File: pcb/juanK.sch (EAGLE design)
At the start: 56 parts, among them IC1 MEGA8-P, IC2 7805TV, T1 2N3904, T2 MCR106, T3 MCR106, T4 MCR106, T5 MCR106, T6 MCR106, T7 MCR106

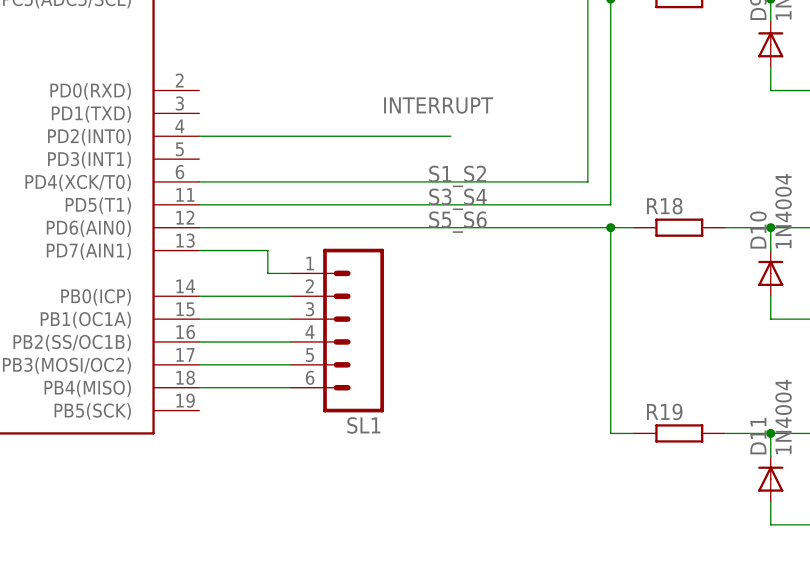
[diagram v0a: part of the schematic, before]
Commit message: Ordenar elementos y Optimizar caminos
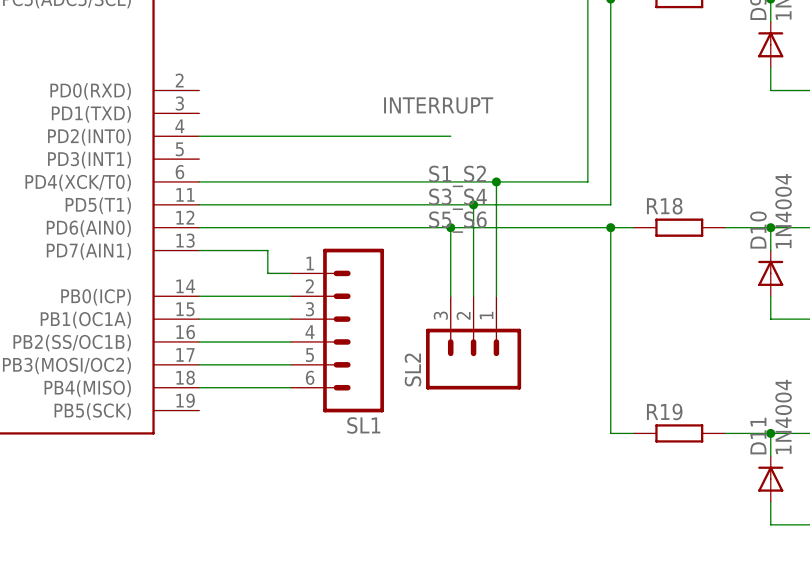
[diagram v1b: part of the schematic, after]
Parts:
- added SL2: (no value), con-amp-quick:M03
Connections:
- net S1_S2: now also SL2.1
- net S3_S4: now also SL2.2
- net S5_S6: now also SL2.3
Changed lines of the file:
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@@
 <?xml version="1.0" encoding="utf-8"?>
 <!DOCTYPE eagle SYSTEM "eagle.dtd">
-<eagle version="6.5.0">
+<eagle version="8.2.2">
 <drawing>
 <settings>
@@
 <grid distance="0.1" unitdist="inch" unit="inch" style="lines" multiple="1" display="no" altdistance="0.01" altunitdist="inch" altunit="inch"/>
 <layers>
-<layer number="1" name="Top" color="4" fill="1" visible="yes" active="no"/>
-<layer number="16" name="Bottom" color="1" fill="1" visible="yes" active="no"/>
-<layer number="17" name="Pads" color="2" fill="1" visible="yes" active="no"/>
-<layer number="18" name="Vias" color="2" fill="1" visible="yes" active="no"/>
-<layer number="19" name="Unrouted" color="6" fill="1" visible="yes" active="no"/>
-<layer number="20" name="Dimension" color="15" fill="1" visible="yes" active="no"/>
-<layer number="21" name="tPlace" color="7" fill="1" visible="yes" active="no"/>
-<layer number="22" name="bPlace" color="7" fill="1" visible="yes" active="no"/>
-<layer number="23" name="tOrigins" color="15" fill="1" visible="yes" active="no"/>
-<layer number="24" name="bOrigins" color="15" fill="1" visible="yes" active="no"/>
-<layer number="25" name="tNames" color="7" fill="1" visible="yes" active="no"/>
-<layer number="26" name="bNames" color="7" fill="1" visible="yes" active="no"/>
-<layer number="27" name="tValues" color="7" fill="1" visible="yes" active="no"/>
-<layer number="28" name="bValues" color="7" fill="1" visible="yes" active="no"/>
+<layer number="1" name="Top" color="4" fill="1" visible="no" active="no"/>
+<layer number="2" name="Route2" color="1" fill="3" visible="no" active="no"/>
+<layer number="3" name="Route3" color="4" fill="3" visible="no" active="no"/>
+<layer number="4" name="Route4" color="1" fill="4" visible="no" active="no"/>
+<layer number="5" name="Route5" color="4" fill="4" visible="no" active="no"/>
+<layer number="6" name="Route6" color="1" fill="8" visible="no" active="no"/>
+<layer number="7" name="Route7" color="4" fill="8" visible="no" active="no"/>
+<layer number="8" name="Route8" color="1" fill="2" visible="no" active="no"/>
+<layer number="9" name="Route9" color="4" fill="2" visible="no" active="no"/>
+<layer number="10" name="Route10" color="1" fill="7" visible="no" active="no"/>
+<layer number="11" name="Route11" color="4" fill="7" visible="no" active="no"/>
+<layer number="12" name="Route12" color="1" fill="5" visible="no" active="no"/>
+<layer number="13" name="Route13" color="4" fill="5" visible="no" active="no"/>
+<layer number="14" name="Route14" color="1" fill="6" visible="no" active="no"/>
+<layer number="15" name="Route15" color="4" fill="6" visible="no" active="no"/>
+<layer number="16" name="Bottom" color="1" fill="1" visible="no" active="no"/>
+<layer number="17" name="Pads" color="2" fill="1" visible="no" active="no"/>
+<layer number="18" name="Vias" color="2" fill="1" visible="no" active="no"/>
+<layer number="19" name="Unrouted" color="6" fill="1" visible="no" active="no"/>
+<layer number="20" name="Dimension" color="15" fill="1" visible="no" active="no"/>
+<layer number="21" name="tPlace" color="7" fill="1" visible="no" active="no"/>
+<layer number="22" name="bPlace" color="7" fill="1" visible="no" active="no"/>
+<layer number="23" name="tOrigins" color="15" fill="1" visible="no" active="no"/>
+<layer number="24" name="bOrigins" color="15" fill="1" visible="no" active="no"/>
+<layer number="25" name="tNames" color="7" fill="1" visible="no" active="no"/>
+<layer number="26" name="bNames" color="7" fill="1" visible="no" active="no"/>
+<layer number="27" name="tValues" color="7" fill="1" visible="no" active="no"/>
+<layer number="28" name="bValues" color="7" fill="1" visible="no" active="no"/>
 <layer number="29" name="tStop" color="7" fill="3" visible="no" active="no"/>
 <layer number="30" name="bStop" color="7" fill="6" visible="no" active="no"/>
@@
 <layer number="35" name="tGlue" color="7" fill="4" visible="no" active="no"/>
 <layer number="36" name="bGlue" color="7" fill="5" visible="no" active="no"/>
-<layer number="37" name="tTest" color="7" fill="1" visible="yes" active="no"/>
-<layer number="38" name="bTest" color="7" fill="1" visible="yes" active="no"/>
+<layer number="37" name="tTest" color="7" fill="1" visible="no" active="no"/>
+<layer number="38" name="bTest" color="7" fill="1" visible="no" active="no"/>
 <layer number="39" name="tKeepout" color="4" fill="11" visible="no" active="no"/>
 <layer number="40" name="bKeepout" color="1" fill="11" visible="no" active="no"/>
@@
 <layer number="44" name="Drills" color="7" fill="1" visible="no" active="no"/>
 <layer number="45" name="Holes" color="7" fill="1" visible="no" active="no"/>
-<layer number="46" name="Milling" color="3" fill="1" visible="yes" active="no"/>
-<layer number="47" name="Measures" color="7" fill="1" visible="yes" active="no"/>
-<layer number="48" name="Document" color="7" fill="1" visible="yes" active="no"/>
-<layer number="49" name="Reference" color="7" fill="1" visible="yes" active="no"/>
-<layer number="51" name="tDocu" color="7" fill="1" visible="yes" active="no"/>
-<layer number="52" name="bDocu" color="7" fill="1" visible="yes" active="no"/>
+<layer number="46" name="Milling" color="3" fill="1" visible="no" active="no"/>
+<layer number="47" name="Measures" color="7" fill="1" visible="no" active="no"/>
+<layer number="48" name="Document" color="7" fill="1" visible="no" active="no"/>
+<layer number="49" name="Reference" color="7" fill="1" visible="no" active="no"/>
+<layer number="51" name="tDocu" color="7" fill="1" visible="no" active="no"/>
+<layer number="52" name="bDocu" color="7" fill="1" visible="no" active="no"/>
 <layer number="90" name="Modules" color="5" fill="1" visible="yes" active="yes"/>
 <layer number="91" name="Nets" color="2" fill="1" visible="yes" active="yes"/>
@@
 <part name="D5" library="diode" deviceset="1N4004" device=""/>
 <part name="IC2" library="linear" deviceset="78*" device="TV" technology="05"/>
-<part name="C5" library="rcl" deviceset="CPOL-EU" device="E5-10.5"/>
+<part name="C5" library="rcl" library_urn="urn:adsk.eagle:library:334" deviceset="CPOL-EU" device="E5-10.5"/>
 <part name="C6" library="rcl" deviceset="C-EU" device="025-025X050"/>
 <part name="GND5" library="supply1" deviceset="GND" device=""/>
@@
 <part name="J2" library="con-amp" deviceset="MTA02-100" device=""/>
 <part name="SL1" library="con-amp-quick" deviceset="M06" device=""/>
+<part name="SL2" library="con-amp-quick" library_urn="urn:adsk.eagle:library:125" deviceset="M03" device=""/>
 </parts>
 <sheets>
@@
 <instance part="J2" gate="G$1" x="134.62" y="147.32"/>
 <instance part="SL1" gate="G$1" x="-5.08" y="12.7" rot="R180"/>
+<instance part="SL2" gate="G$1" x="10.16" y="7.62" rot="R90"/>
 </instances>
 <busses>
@@
 <segment>
 <pinref part="IC1" gate="G$1" pin="PD4(XCK/T0)"/>
-<wire x1="-20.32" y1="27.94" x2="22.86" y2="27.94" width="0.1524" layer="91"/>
+<wire x1="-20.32" y1="27.94" x2="12.7" y2="27.94" width="0.1524" layer="91"/>
 <label x="5.08" y="27.94" size="1.778" layer="95"/>
 <pinref part="R14" gate="G$1" pin="1"/>
+<wire x1="12.7" y1="27.94" x2="22.86" y2="27.94" width="0.1524" layer="91"/>
 <wire x1="27.94" y1="119.38" x2="25.4" y2="119.38" width="0.1524" layer="91"/>
 <pinref part="R15" gate="G$1" pin="1"/>
@@
 <junction x="25.4" y="96.52"/>
 <wire x1="22.86" y1="96.52" x2="22.86" y2="27.94" width="0.1524" layer="91"/>
+<pinref part="SL2" gate="G$1" pin="1"/>
+<wire x1="12.7" y1="15.24" x2="12.7" y2="27.94" width="0.1524" layer="91"/>
+<junction x="12.7" y="27.94"/>
 </segment>
 </net>
@@
 <segment>
 <pinref part="IC1" gate="G$1" pin="PD5(T1)"/>
-<wire x1="-20.32" y1="25.4" x2="25.4" y2="25.4" width="0.1524" layer="91"/>
+<wire x1="-20.32" y1="25.4" x2="10.16" y2="25.4" width="0.1524" layer="91"/>
 <label x="5.08" y="25.4" size="1.778" layer="95"/>
 <pinref part="R16" gate="G$1" pin="1"/>
+<wire x1="10.16" y1="25.4" x2="25.4" y2="25.4" width="0.1524" layer="91"/>
 <wire x1="27.94" y1="71.12" x2="25.4" y2="71.12" width="0.1524" layer="91"/>
 <pinref part="R17" gate="G$1" pin="1"/>
@@
 <wire x1="25.4" y1="25.4" x2="25.4" y2="48.26" width="0.1524" layer="91"/>
 <junction x="25.4" y="48.26"/>
+<pinref part="SL2" gate="G$1" pin="2"/>
+<wire x1="10.16" y1="15.24" x2="10.16" y2="25.4" width="0.1524" layer="91"/>
+<junction x="10.16" y="25.4"/>
 </segment>
 </net>
@@
 <segment>
 <pinref part="IC1" gate="G$1" pin="PD6(AIN0)"/>
-<wire x1="-20.32" y1="22.86" x2="25.4" y2="22.86" width="0.1524" layer="91"/>
+<wire x1="-20.32" y1="22.86" x2="7.62" y2="22.86" width="0.1524" layer="91"/>
 <label x="5.08" y="22.86" size="1.778" layer="95"/>
 <pinref part="R18" gate="G$1" pin="1"/>
 <pinref part="R19" gate="G$1" pin="1"/>
+<wire x1="7.62" y1="22.86" x2="25.4" y2="22.86" width="0.1524" layer="91"/>
 <wire x1="25.4" y1="22.86" x2="27.94" y2="22.86" width="0.1524" layer="91"/>
 <wire x1="27.94" y1="0" x2="25.4" y2="0" width="0.1524" layer="91"/>
 <wire x1="25.4" y1="0" x2="25.4" y2="22.86" width="0.1524" layer="91"/>
 <junction x="25.4" y="22.86"/>
+<pinref part="SL2" gate="G$1" pin="3"/>
+<wire x1="7.62" y1="15.24" x2="7.62" y2="22.86" width="0.1524" layer="91"/>
+<junction x="7.62" y="22.86"/>
 </segment>
 </net>
@@
 </schematic>
 </drawing>
+<compatibility>
+<note version="8.2" severity="warning">
+Since Version 8.2, Eagle supports online libraries. The ids
+of those online libraries will not be understood (or retained)
+with this version.
+</note>
+</compatibility>
 </eagle>

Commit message: Diseño de PCB terminado
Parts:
- added JP1, JP10, JP11, JP12, JP13, JP14, JP15, JP16, JP17, JP18, JP19, JP2, JP20, JP21, JP22, JP23, JP24, JP3, JP4, JP5, JP6, JP7, JP8, JP9: (no value), pinhead:PINHD-1X1
- J1, J2: device con-amp:MTA02-100 -> con-lstb:MA03-1
- SL1: device con-amp-quick:M06 -> con-amp:MTA06-100
- SL2: device con-amp-quick:M03 -> con-amp:MTA04-100
- T2, T3, T4, T5, T6, T7: value MCR106 -> TIC106S; device triac:MCR106 -> triac:TIC106S
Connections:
- removed net N$13: T2.C, T4.C, T6.C
- new net VO: JP23.1, JP24.1, T2.C, T4.C, T6.C
- net A: now also JP15.1, JP16.1
- net B: now also J2.3, JP11.1, JP12.1, JP17.1, JP18.1; no longer J2.2
- net C: now also JP19.1, JP20.1
- net GND: now also JP13.1, JP14.1, SL2.4
- net GND1: now also JP21.1, JP22.1
- net N$11: now also J1.3; no longer J1.2
- net N$22: now also JP5.1, JP6.1
- net N$24: now also JP7.1, JP8.1
- net N$25: now also JP3.1, JP4.1
- net N$6: now also JP10.1, JP9.1
- net N$8: now also JP1.1, JP2.1
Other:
- moved on the sheet: SL2

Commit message: Corregir dimensiones de algunos componentes
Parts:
- removed J1, J2: (no value), con-lstb:MA03-1
- added LED1: (no value), led:LED3MM
- added R20: (no value), rcl:R-EU_0204/5
- added X1, X2: (no value), con-wago-500:W237-102
- Q1: device crystal:CRYSTALTC26V -> crystal:CRYSTALHC49U70
- R2: device pot:TRIM_EU-B64Y -> pot:3RP/1610N
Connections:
- new net N$13: LED1.A, R20.1
- net 5V: now also R2.E, R20.2; no longer R2.A
- net A: now also X2-1.KL; no longer J2.1
- net B: now also X2-2.KL; no longer J2.3
- net GND: now also LED1.C, R2.A; no longer R2.E
- net N$10: now also X1-1.KL; no longer J1.1
- net N$11: now also X1-2.KL; no longer J1.3
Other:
- moved on the sheet: C5, C6, D5, IC2, R7
